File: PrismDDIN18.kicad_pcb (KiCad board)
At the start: 2 copper layers, 280 x 60 mm, 90 parts, among them CON1 BARREL_JACK, IC1 LM2596T-5, J1 Conn_01x03, M1 IN-18, M10 IN-18, Q2 2N7000, Q3 2N7000, Q4 2N7000, Q5 2N7000, Q6 IRF540N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

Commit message: Update IN-18 footprints, define RV1 value
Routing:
- net /VCC: track 764.0 -> 763.8 mm, vias 10 -> 9
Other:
- board text added: "Data 5V GND"
- board text added: "NeoPixel Test Point"

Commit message: Re-center connections to tubes
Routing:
- net /M1_5: track 56.1 -> 59.2 mm
- net /M1_4: track 53.3 -> 55.7 mm
- net /H10_8: track 76.0 -> 77.6 mm
- net /S10_8: track 60.8 -> 62.2 mm
- net /M10_4: track 40.8 -> 39.6 mm
- net /S10_2: track 64.7 -> 65.7 mm
- net /S10_0: track 41.0 -> 41.9 mm
- net /M1_2: track 23.2 -> 24.1 mm
- net /S10_9: track 40.4 -> 41.2 mm
- net /S1_9: track 68.9 -> 69.7 mm
- net /S1_0: track 69.0 -> 69.6 mm
- net /S1_8: track 85.9 -> 86.4 mm
- net /M10_5: track 42.4 -> 41.9 mm

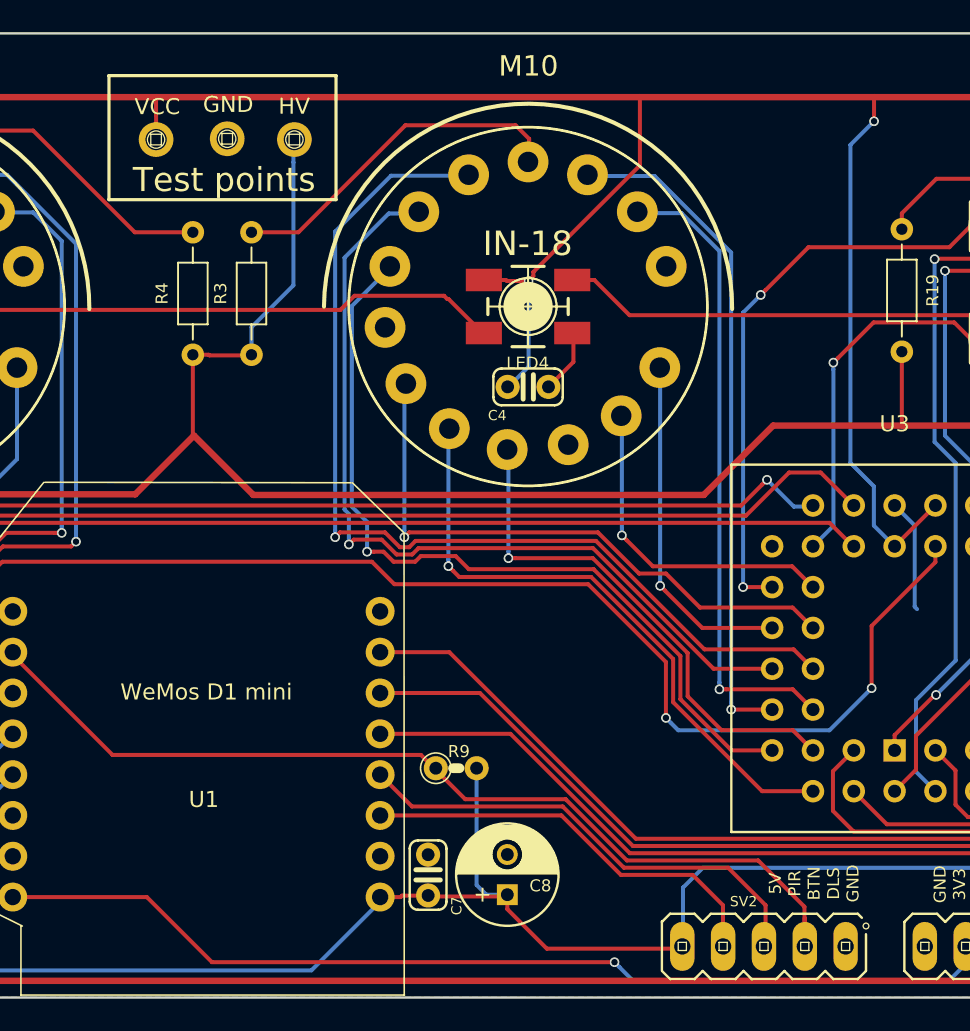
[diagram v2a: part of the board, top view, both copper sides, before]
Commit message: Add 3V3 test point, move test points
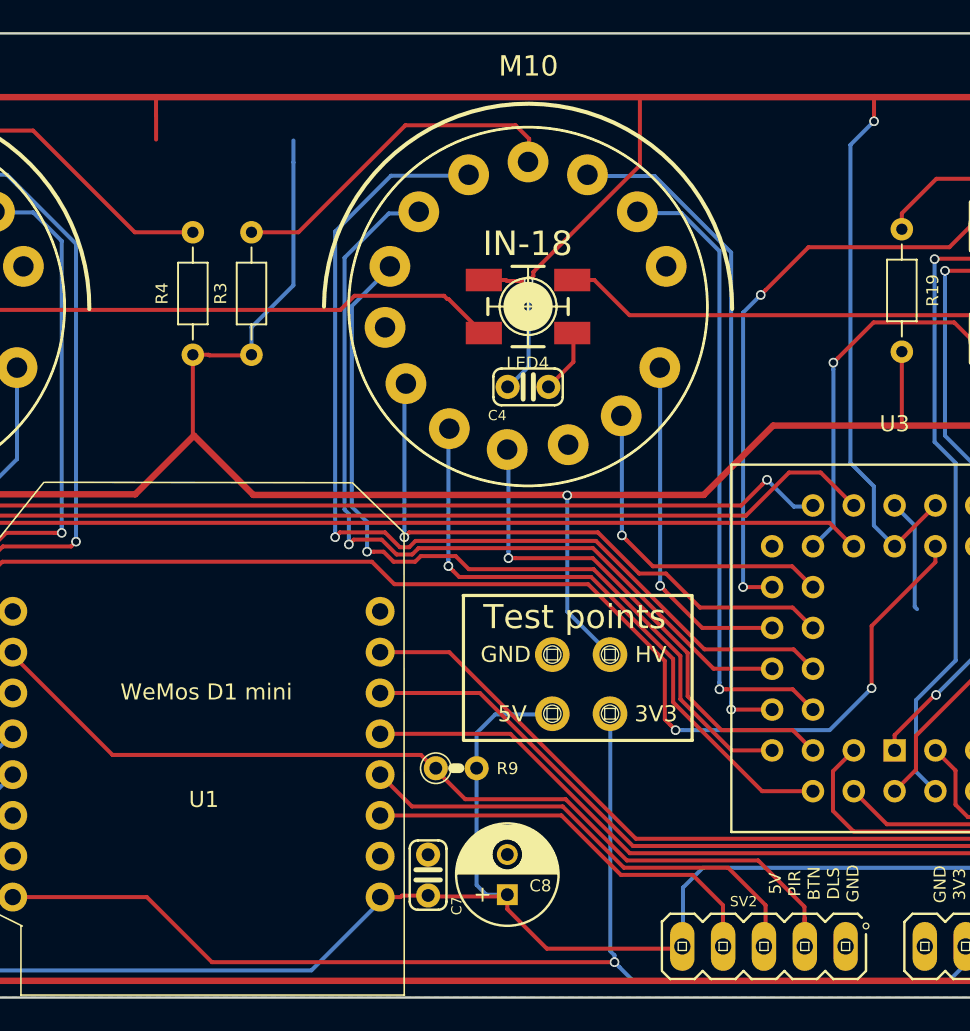
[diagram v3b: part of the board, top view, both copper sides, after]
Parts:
- added W4: 3V3, NixieClockMaster:TESTPAD_P1-13, F.Cu at (245.1, 148.3)
- RV1: value POT -> 1k
- W1: value VCC -> 5V
- moved W1 43.4 mm to (241.5, 148.3)
- moved W2 37.9 mm to (241.5, 144.7)
- moved W3 37.6 mm to (245.1, 144.7)
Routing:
- net /3V3: track 127.8 -> 143.4 mm
- net /HV: track 357.3 -> 368.2 mm, vias 2 -> 3
- net /VCC: track 763.8 -> 771.5 mm

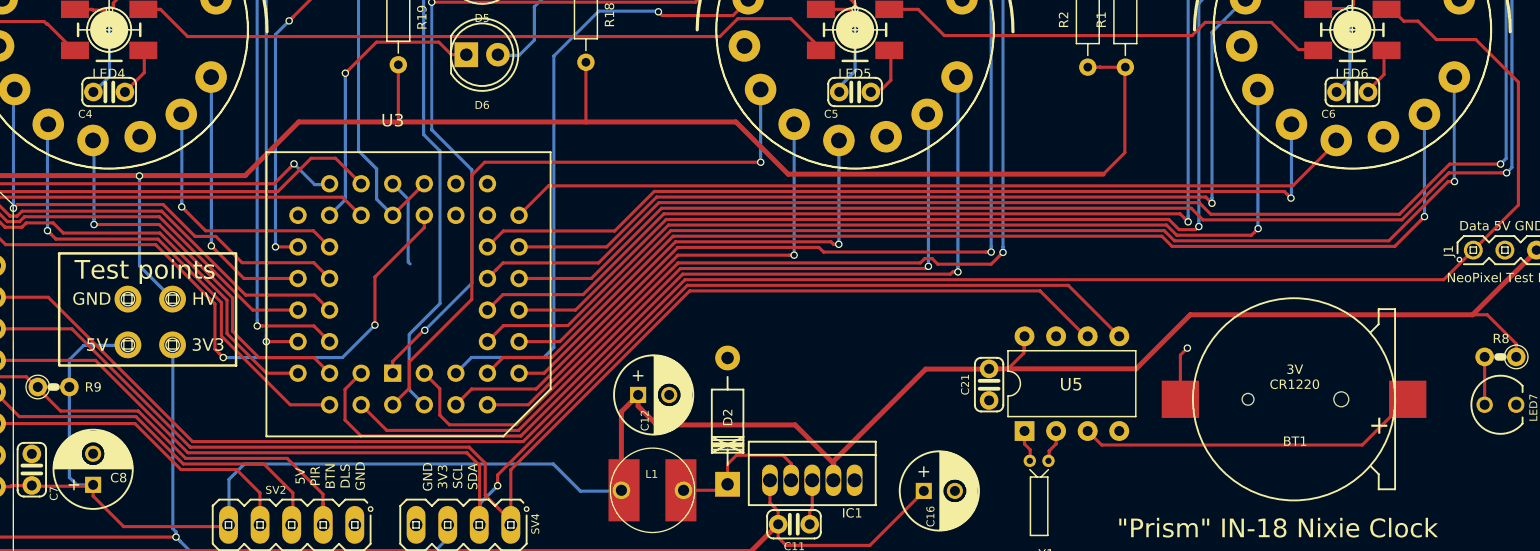
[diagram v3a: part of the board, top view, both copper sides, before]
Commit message: Add I2C pullups
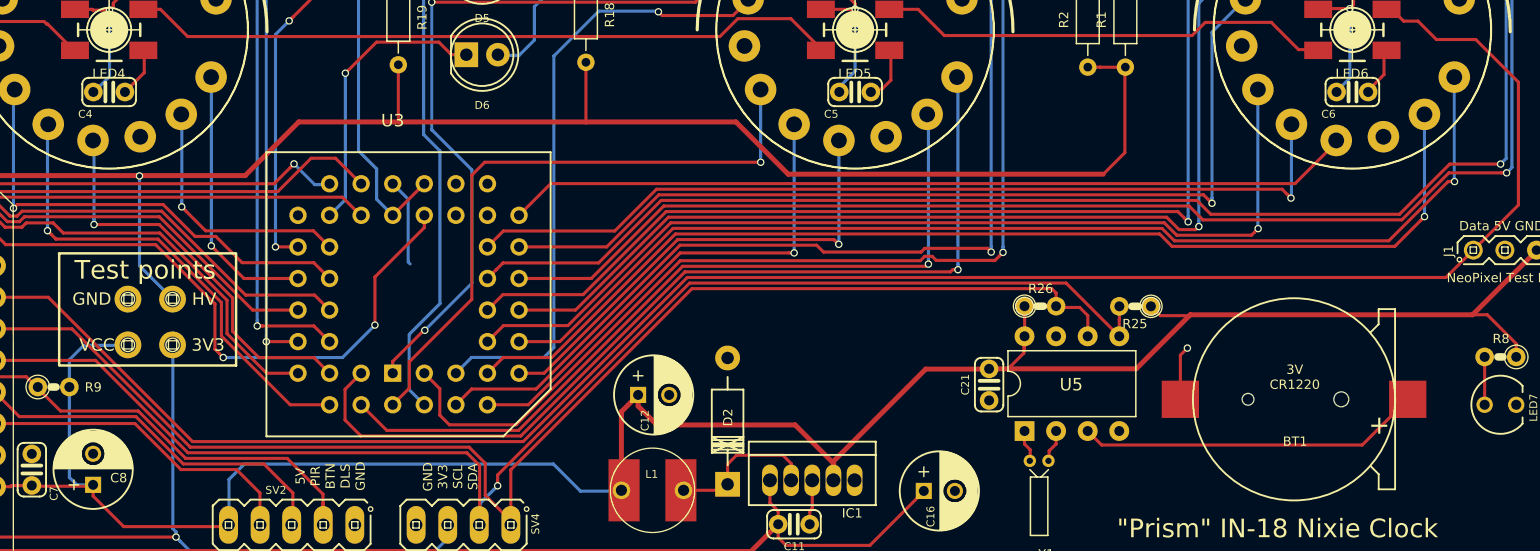
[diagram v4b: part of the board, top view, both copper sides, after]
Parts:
- added R25: 10k, NixieClockMaster:R-0207_2V, F.Cu at (322.5, 145.2)
- added R26: 10k, NixieClockMaster:R-0207_2V, F.Cu at (314.9, 145.2)
- W1: value 5V -> VCC
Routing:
- net /VCC: track 771.5 -> 777.4 mm
- net /SDA: track 109.9 -> 112.5 mm
- net /SCL: track 108.4 -> 110.0 mm

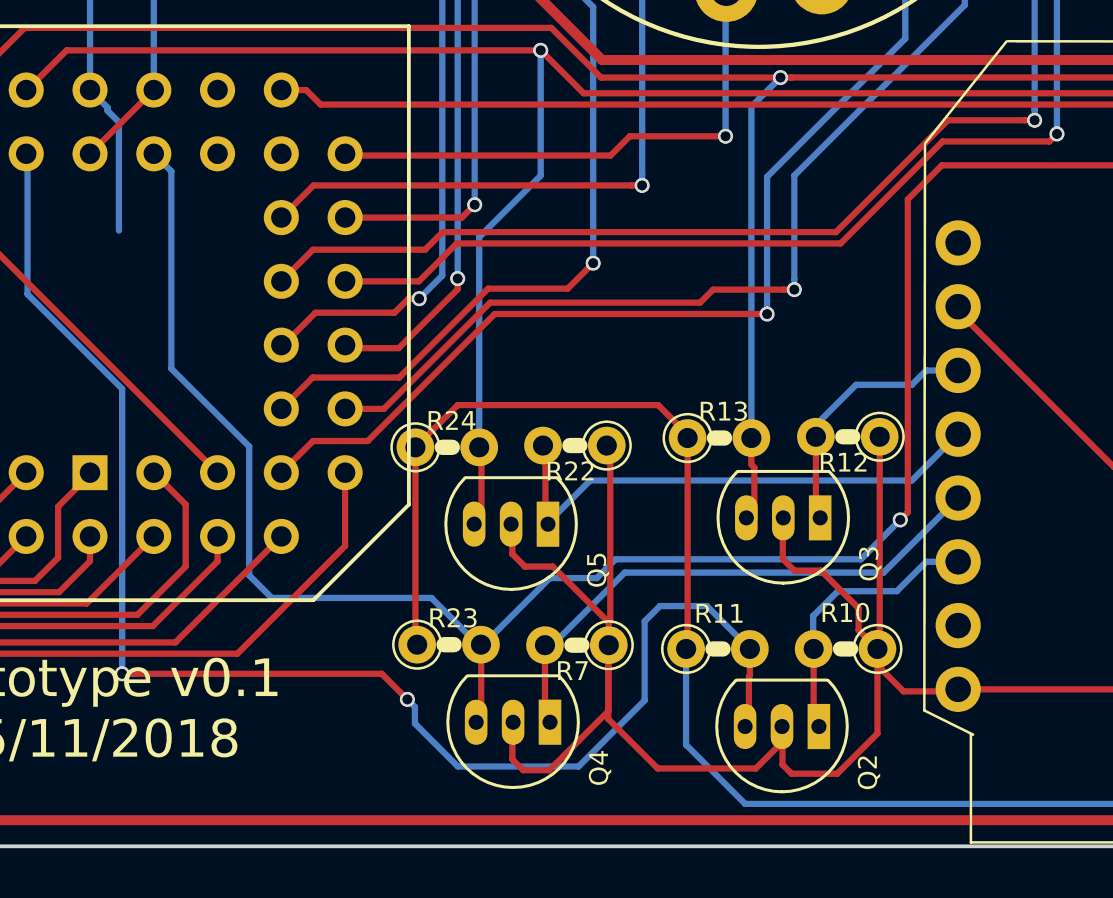
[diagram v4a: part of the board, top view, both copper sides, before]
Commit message: Minor adjustments to level shifter placings
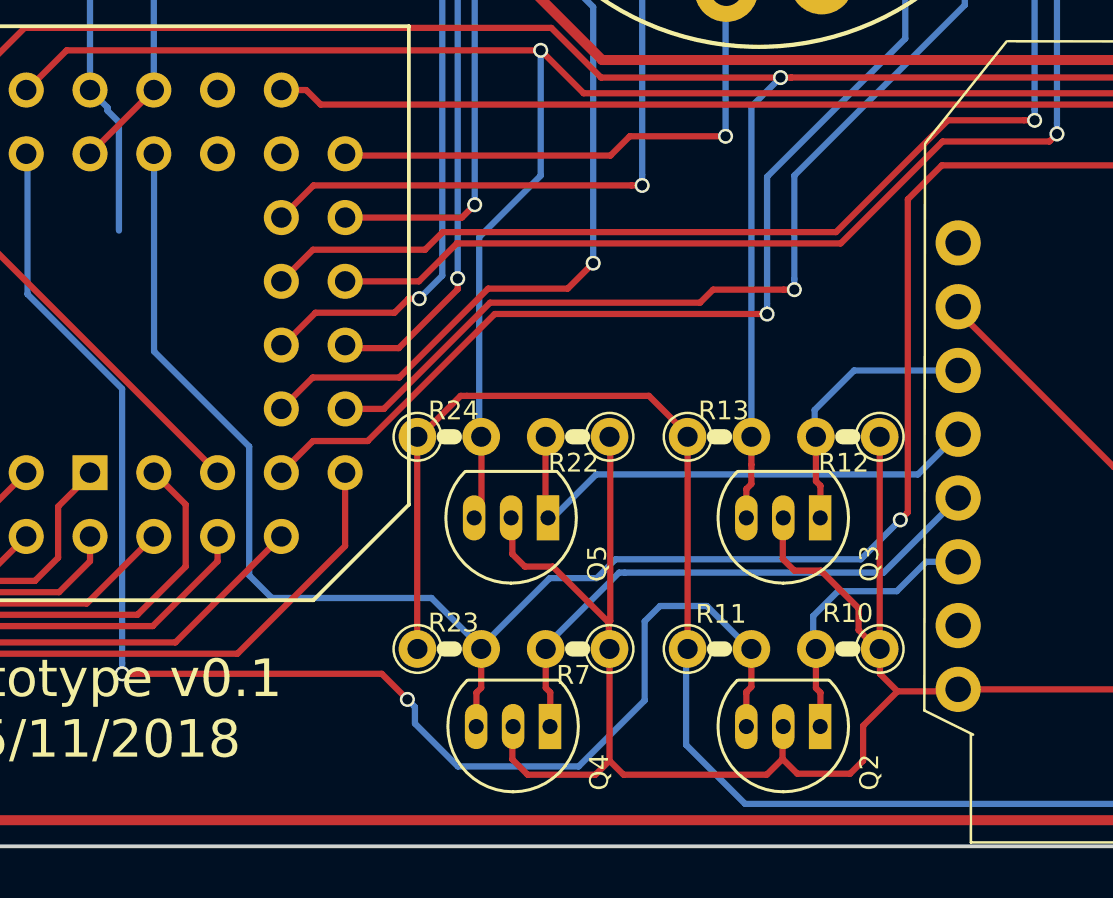
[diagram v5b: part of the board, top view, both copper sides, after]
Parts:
- moved R24 0.43 mm to (187.7, 149.7)
- moved R22 0.37 mm to (192.8, 149.7)
- moved Q5 0.25 mm to (191.4, 152.9)
- moved R23 0.17 mm to (187.7, 158.1)
- moved Q4 0.17 mm to (191.5, 161.2)
- moved R7 0.15 mm to (192.8, 158.1)
- moved R10 0.09 mm to (203.5, 158.1)
- moved R11 0.06 mm to (198.4, 158.1)
- moved Q2 0.05 mm to (202.2, 161.2)
- moved R13 0.05 mm to (198.4, 149.7)
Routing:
- net /3V3: track 143.4 -> 140.0 mm
- net /VCC: track 777.4 -> 778.1 mm
- net /CLK: track 137.4 -> 137.9 mm
